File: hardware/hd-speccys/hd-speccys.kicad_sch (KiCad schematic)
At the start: 52 parts, among them J1 9-20VDC, J2 PI_ZERO, J3 ULA_SOCKET, J4 ULA_ZX, J5 UART, J6 Debug_Data, J7 Debug_Ctrl, J8 PWR_OUT, U1 74LS541, U2 74LS541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

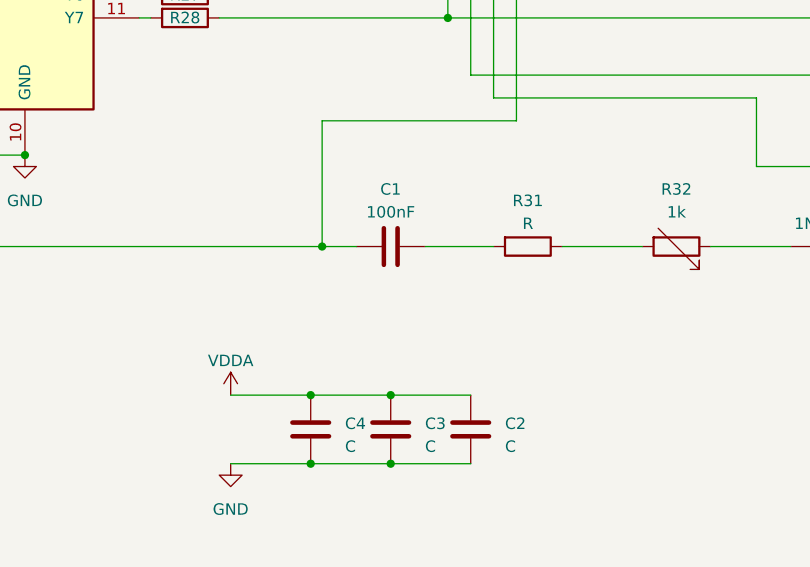
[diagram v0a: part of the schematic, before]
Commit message: feat: add TZX, TAP, etc playback with TZXDuino code - working - tested lots of titles and loaders. Later buffer underrun will likely be an issue (it is already with BackToSkool) - not sure why buffer cannot be made larger at present.
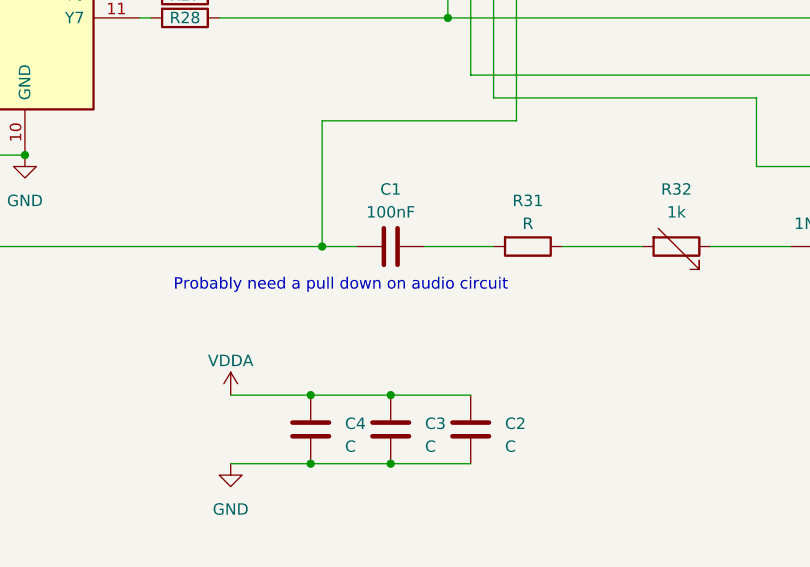
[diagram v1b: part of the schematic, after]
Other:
- note added: "Probably need a pull down on audio circuit"
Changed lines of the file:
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@@
     (stroke (width 0) (type default))
+  )
+  (text "Probably need a pull down on audio circuit" (at 132.08 163.83 0)
+    (effects (font (size 1.27 1.27)) (justify left bottom))
   )
   (symbol (lib_id "power:GND") (at 81.28 35.56 0) (unit 1)

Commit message: hw: PCB modifications - route between ULA pins and socket efficiently
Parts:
- removed C1: 100nF, Capacitor_SMD:C_0603_1608Metric_Pad1.08x0.95mm_HandSolder, symbol Device:C
- removed D1, D2, D3: 1N4148, Diode_SMD:D_SOD-323_HandSoldering, symbol Diode:1N4148
- removed R20, R29: R, Resistor_SMD:R_0603_1608Metric_Pad0.98x0.95mm_HandSolder, symbol Device:R
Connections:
- net at J2.26 (SWE_SRW_(GPIO7)), J6.10 (AUDIO): now also R32.1
- net at J6.3 (D2), R23.1: now also J2.12 (SD10); no longer J2.40 (SD13)
- net at J6.1 (D0), R21.1: now also J2.36 (SD8); no longer J2.16 (SD15)
- net at J3.28 (MIC_TAPE), J4.28 (MIC_TAPE), J6.11 (MIC_TAPE): now also R31.2
- net at J6.2 (D1), R22.1: now also J2.11 (SD9); no longer J2.15 (SD14)
- net at J6.4 (D3), R24.1: now also J2.35 (SD11); no longer J2.38 (SD12)
- net at J6.5 (D4), R25.1: now also J2.38 (SD12); no longer J2.35 (SD11)
- net at J6.6 (D5), R26.1: now also J2.40 (SD13); no longer J2.12 (SD10)
- net at J6.7 (D6), R27.1: now also J2.15 (SD14); no longer J2.11 (SD9)
- net at J6.8 (D7), R28.1: now also J2.16 (SD15); no longer J2.36 (SD8)
- net at J7.2 (/IO_WR), U5.4: now also J2.37 (GPIO26)
- net at J2.13 (GPIO27), J7.6 (/INT): now also U1.11 (Y7), U3.13
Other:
- note added: "TODO: Define these values based on testing TODO: Add reset control TODO: Add +/- terminals to silkscreen TODO: Check grounding (don't connect wrong GNDs together)"
- note removed: "Probably need a pull down on audio circuit"
